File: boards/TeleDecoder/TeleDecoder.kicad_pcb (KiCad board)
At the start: 4 copper layers, 40 x 40 mm, 63 parts, among them J1 Conn_01x02, J101 USB4105-GF-A, J2 Conn_Coaxial, J3 Conn_01x03, U1 ESP32-S3-MINI-1U, U2 TPS746-Q1, U3 CC1120, U4 ECMF02-2AMX6, Y1 STDCZS3-40M

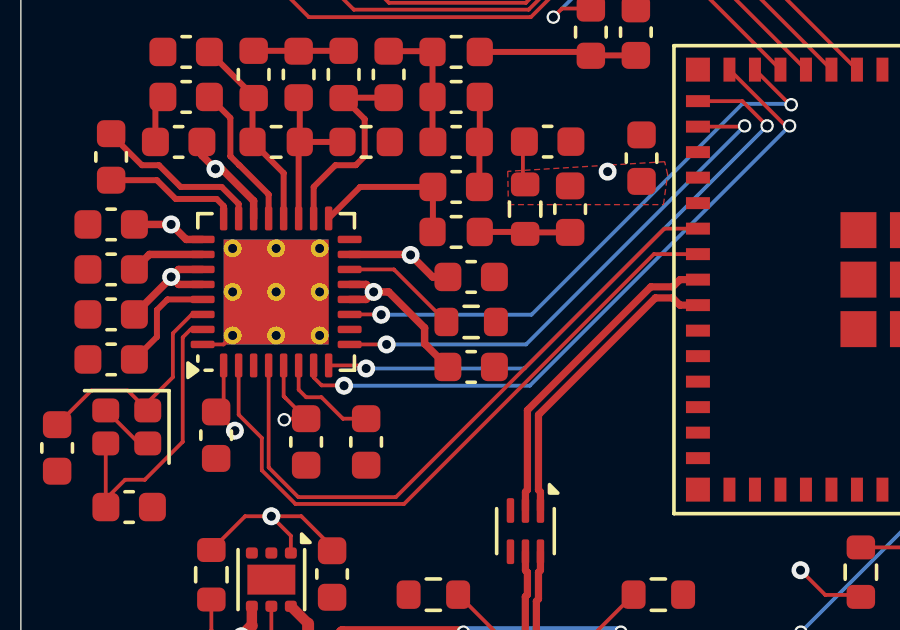
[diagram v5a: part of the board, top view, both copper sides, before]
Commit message: Decoupling capacitor
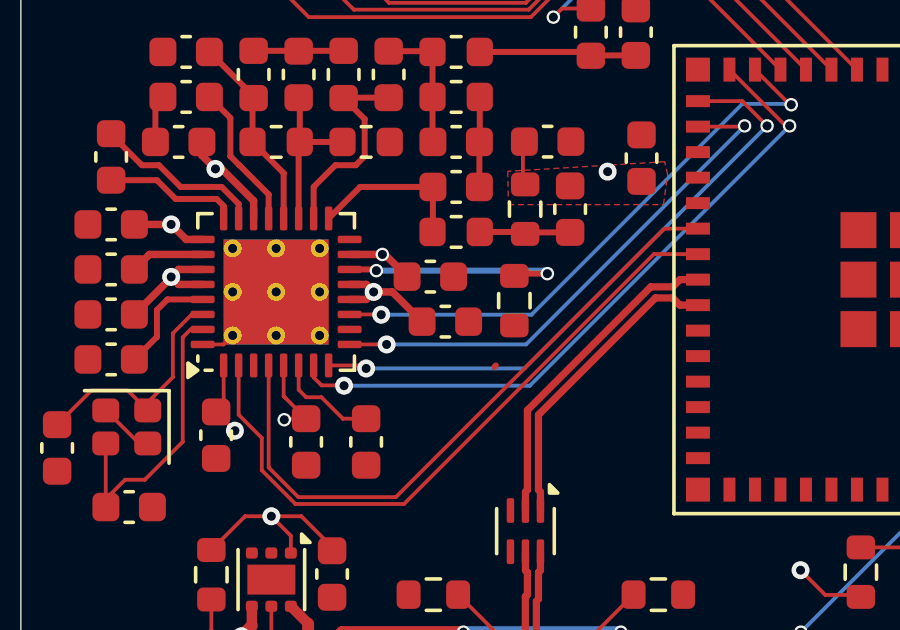
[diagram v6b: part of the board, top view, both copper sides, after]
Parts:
- moved C15 1.74 mm to (82.4, 71.9)
- moved R2 1.61 mm to (84.7, 71.2), turned to -90 degrees
- moved C14 1.36 mm to (81.9, 70.4)
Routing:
- net Net-(U3-RBIAS): track 3.95 -> 7.78 mm, vias 0 -> 2
- net +3V3: track 38.6 -> 35.4 mm
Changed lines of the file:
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@@
 	(footprint "Capacitor_SMD:C_0603_1608Metric"
 		(layer "F.Cu")
-		(at 83.26 73.41)
+		(at 82.4 71.9)
 		(descr "Capacitor SMD 0603 (1608 Metric), square (rectangular) end terminal, IPC-7351 nominal, (Body size source: IPC-SM-782 page 76, https://www.pcb-3d.com/wordpress/wp-content/uploads/ipc-sm-782a_amendment_1_and_2.pdf), generated with kicad-footprint-generator")
 		(tags "capacitor")
@@
 	(footprint "Capacitor_SMD:C_0603_1608Metric"
 		(layer "F.Cu")
-		(at 83.26 70.41)
+		(at 81.9 70.4)
 		(descr "Capacitor SMD 0603 (1608 Metric), square (rectangular) end terminal, IPC-7351 nominal, (Body size source: IPC-SM-782 page 76, https://www.pcb-3d.com/wordpress/wp-content/uploads/ipc-sm-782a_amendment_1_and_2.pdf), generated with kicad-footprint-generator")
 		(tags "capacitor")
@@
 	(footprint "Resistor_SMD:R_0603_1608Metric"
 		(layer "F.Cu")
-		(at 83.26 71.91)
+		(at 84.7 71.2 -90)
 		(descr "Resistor SMD 0603 (1608 Metric), square (rectangular) end terminal, IPC-7351 nominal, (Body size source: IPC-SM-782 page 72, https://www.pcb-3d.com/wordpress/wp-content/uploads/ipc-sm-782a_amendment_1_and_2.pdf), generated with kicad-footprint-generator")
 		(tags "resistor")
 		(property "Reference" "R2"
-			(at 0 -1.43 0)
+			(at 0 -1.43 90)
 			(layer "F.SilkS")
 			(hide yes)
@@
 		)
 		(property "Value" "56k"
-			(at 0 1.43 0)
+			(at 0 1.43 90)
 			(layer "F.Fab")
 			(effects
@@
 		)
 		(property "Datasheet" "~"
-			(at 0 0 0)
+			(at 0 0 90)
 			(layer "F.Fab")
 			(hide yes)
@@
 		)
 		(property "Description" "Resistor, US symbol"
-			(at 0 0 0)
+			(at 0 0 90)
 			(layer "F.Fab")
 			(hide yes)
@@
 		(attr smd)
 		(fp_line
-			(start -0.237258 -0.5225)
-			(end 0.237258 -0.5225)
+			(start -0.237258 0.5225)
+			(end 0.237258 0.5225)
 			(stroke
 				(width 0.12)
@@
 		)
 		(fp_line
-			(start -0.237258 0.5225)
-			(end 0.237258 0.5225)
+			(start -0.237258 -0.5225)
+			(end 0.237258 -0.5225)
 			(stroke
 				(width 0.12)
@@
 		)
 		(fp_line
-			(start -1.48 -0.73)
-			(end 1.48 -0.73)
+			(start -1.48 0.73)
+			(end -1.48 -0.73)
 			(stroke
 				(width 0.05)
@@
 		)
 		(fp_line
-			(start -1.48 0.73)
-			(end -1.48 -0.73)
+			(start 1.48 0.73)
+			(end -1.48 0.73)
 			(stroke
 				(width 0.05)
@@
 		)
 		(fp_line
-			(start 1.48 -0.73)
-			(end 1.48 0.73)
+			(start -1.48 -0.73)
+			(end 1.48 -0.73)
 			(stroke
 				(width 0.05)
@@
 		)
 		(fp_line
-			(start 1.48 0.73)
-			(end -1.48 0.73)
+			(start 1.48 -0.73)
+			(end 1.48 0.73)
 			(stroke
 				(width 0.05)
@@
 		)
 		(fp_line
-			(start -0.8 -0.4125)
-			(end 0.8 -0.4125)
+			(start -0.8 0.4125)
+			(end -0.8 -0.4125)
 			(stroke
 				(width 0.1)
@@
 		)
 		(fp_line
-			(start -0.8 0.4125)
-			(end -0.8 -0.4125)
+			(start 0.8 0.4125)
+			(end -0.8 0.4125)
 			(stroke
 				(width 0.1)
@@
 		)
 		(fp_line
-			(start 0.8 -0.4125)
-			(end 0.8 0.4125)
+			(start -0.8 -0.4125)
+			(end 0.8 -0.4125)
 			(stroke
 				(width 0.1)
@@
 		)
 		(fp_line
-			(start 0.8 0.4125)
-			(end -0.8 0.4125)
+			(start 0.8 -0.4125)
+			(end 0.8 0.4125)
 			(stroke
 				(width 0.1)
@@
 		)
 		(fp_text user "${REFERENCE}"
-			(at 0 0 0)
+			(at 0 0 90)
 			(layer "F.Fab")
 			(effects
@@
 		)
 		(pad "1" smd roundrect
-			(at -0.825 0)
+			(at -0.825 0 270)
 			(size 0.8 0.95)
 			(layers "F.Cu" "F.Mask" "F.Paste")
@@
 		)
 		(pad "2" smd roundrect
-			(at 0.825 0)
+			(at 0.825 0 270)
 			(size 0.8 0.95)
 			(layers "F.Cu" "F.Mask" "F.Paste")
@@
 	)
 	(segment
-		(start 84.035 71.86)
-		(end 84.085 71.91)
-		(width 0.2)
-		(layer "F.Cu")
-		(net 1)
-	)
-	(segment
 		(start 75.01 72.66)
 		(end 75.31 72.36)
@@
 	)
 	(segment
-		(start 81.709 72.109)
-		(end 81.709 72.634)
-		(width 0.25)
-		(layer "F.Cu")
-		(net 10)
-	)
-	(segment
-		(start 81.709 72.634)
-		(end 82.485 73.41)
+		(start 79.21 69.66)
+		(end 80.3 69.66)
 		(width 0.25)
 		(layer "F.Cu")
@@
 	)
 	(segment
-		(start 81.224972 69.66)
-		(end 81.242429 69.677457)
+		(start 80.635 70.91)
+		(end 81.625 71.9)
 		(width 0.25)
 		(layer "F.Cu")
@@
 	)
 	(segment
-		(start 79.21 69.66)
-		(end 81.224972 69.66)
-		(width 0.25)
-		(layer "F.Cu")
-		(net 10)
-	)
-	(segment
 		(start 76.01 68.46)
 		(end 76.01 67.874647)
@@
 	)
 	(segment
-		(start 80.51 70.91)
-		(end 81.709 72.109)
+		(start 80.385 69.66)
+		(end 81.125 70.4)
 		(width 0.25)
 		(layer "F.Cu")
@@
 	)
 	(segment
-		(start 80.01 70.91)
-		(end 80.51 70.91)
-		(width 0.25)
-		(layer "F.Cu")
-		(net 10)
-	)
-	(segment
 		(start 95.065 81.01)
 		(end 94.24 80.185)
@@
 	)
 	(segment
-		(start 82.485 73.385)
-		(end 82.485 73.41)
-		(width 0.25)
-		(layer "F.Cu")
-		(net 10)
-	)
-	(segment
 		(start 77.6 78.3875)
 		(end 76.6 78.3875)
@@
 	)
 	(segment
-		(start 81.242429 69.677457)
-		(end 81.974972 70.41)
+		(start 80.01 70.91)
+		(end 80.635 70.91)
 		(width 0.25)
 		(layer "F.Cu")
@@
 	)
 	(segment
-		(start 81.974972 70.41)
-		(end 82.485 70.41)
-		(width 0.25)
+		(start 77.76 75.135)
+		(end 77.065 75.135)
+		(width 0.127)
 		(layer "F.Cu")
 		(net 10)
 	)
 	(segment
-		(start 77.76 75.135)
-		(end 77.065 75.135)
-		(width 0.127)
+		(start 80.3 69.66)
+		(end 80.385 69.66)
+		(width 0.25)
 		(layer "F.Cu")
 		(net 10)
 	)
 	(via
+		(at 80.3 69.66)
+		(size 0.45)
+		(drill 0.3)
+		(layers "F.Cu" "B.Cu")
+		(net 10)
+	)
+	(via
 		(at 74.736778 66.81)
 		(size 0.6)
@@
 	)
 	(via
-		(at 81.242429 69.677457)
-		(size 0.6)
-		(drill 0.3)
-		(layers "F.Cu" "B.Cu")
-		(free yes)
-		(net 10)
-	)
-	(via
 		(at 73.26 70.41)
 		(size 0.6)
@@
 	)
 	(segment
-		(start 80.685 70.16)
-		(end 82.435 71.91)
-		(width 0.127)
+		(start 85.8 70.3)
+		(end 84.775 70.3)
+		(width 0.2)
 		(layer "F.Cu")
 		(net 30)
@@
 	(segment
 		(start 79.21 70.16)
-		(end 80.685 70.16)
-		(width 0.127)
+		(end 80.06 70.16)
+		(width 0.2)
+		(layer "F.Cu")
+		(net 30)
+	)
+	(segment
+		(start 80.06 70.16)
+		(end 80.1 70.2)
+		(width 0.2)
+		(layer "F.Cu")
+		(net 30)
+	)
+	(segment
+		(start 84.775 70.3)
+		(end 84.7 70.375)
+		(width 0.2)
 		(layer "F.Cu")
 		(net 30)
 	)
+	(via
+		(at 80.1 70.2)
+		(size 0.45)
+		(drill 0.3)
+		(layers "F.Cu" "B.Cu")
+		(net 30)
+	)
+	(via
+		(at 85.8 70.3)
+		(size 0.45)
+		(drill 0.3)
+		(layers "F.Cu" "B.Cu")
+		(net 30)
+	)
+	(segment
+		(start 85.7 70.2)
+		(end 85.8 70.3)
+		(width 0.2)
+		(layer "B.Cu")
+		(net 30)
+	)
+	(segment
+		(start 80.1 70.2)
+		(end 85.7 70.2)
+		(width 0.2)
+		(layer "B.Cu")
+		(net 30)
+	)

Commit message: drawings
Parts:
- added G***: LOGO, Logos_ISS:ISS_LOGO_even more extreme small, F.Cu at (96.5, 60.2)
- moved C24 4.95 mm to (104.7, 59.7), turned to 0 degrees
- moved C25 1.70 mm to (104.7, 61.2)
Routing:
- net +3V3: track 35.4 -> 36.2 mm
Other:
- board text added: "Benson Zhou, Kevin Zhao, Himesh Nasaka"
- board text added: "TeleDecoder"

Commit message: grainger logo
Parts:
- added G***: LOGO, memes:Grainger_small, F.Cu at (99.0, 81.3)
- J2: footprint Connector_Coax:SMA_Molex_732511153_EdgeMount_Horizontal -> Connector_Coax:SMA_Molex_73251-2120_EdgeMount_Horizontal
- moved R10 12.1 mm to (106.8, 74.2), turned to 90 degrees
- moved C28 9.01 mm to (106.8, 77.2)
- moved R4 2.14 mm to (87.5, 80.2), turned to 90 degrees
- moved J2 2.08 mm to (88.2, 53.5), turned to 90 degrees
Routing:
- net +3V3: track 36.2 -> 35.1 mm
- net /RESET: track 16.1 -> 17.1 mm
- net Net-(J101-CC2): track 3.06 -> 2.49 mm
